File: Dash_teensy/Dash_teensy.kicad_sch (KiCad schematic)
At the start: 72 parts, among them J1 J1B1211CCD, J10 2060-452_998-404, J11 2060-452_998-404, J12 J1B1211CCD, J13 BM04B-GHS-TBT_LF__SN_, J14 BM04B-GHS-TBT_LF__SN_, J15 2060-452_998-404, J2 2060-452_998-404, J3 2060-452_998-404, J4 2060-452_998-404, J5 2060-452_998-404, J6 2060-452_998-404, J7 2060-452_998-404, J8 J1B1211CCD, J9 2060-452_998-404, U1 DEV-16771, U10 MCP2562FDT-E/SN, U11 MCP2562FDT-E/SN, U12 MCP2562FDT-E/SN, U2 DEV-16771, U3 DEV-16771, U4 MCP2562FDT-E/SN, U5 MCP2562FDT-E/SN, U6 MCP2562FDT-E/SN, U7 MCP2562FDT-E/SN, U8 MCP2562FDT-E/SN, U9 MCP2562FDT-E/SN

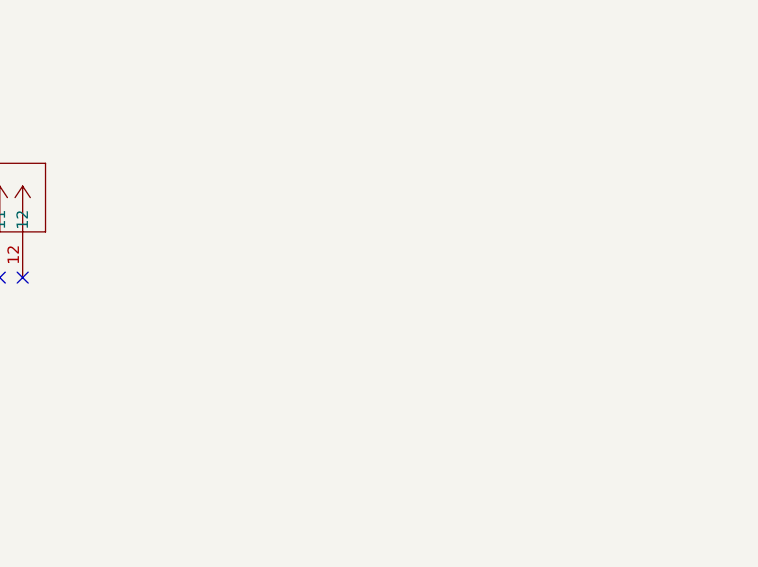
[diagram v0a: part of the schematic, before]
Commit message: figured out placement
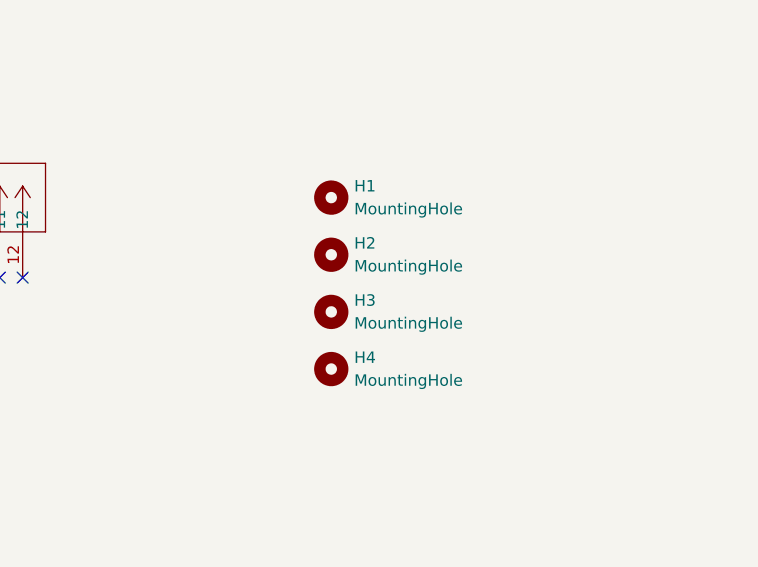
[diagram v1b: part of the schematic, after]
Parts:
- added H1, H2, H3, H4: MountingHole, MountingHole:MountingHole_3.2mm_M3_DIN965_Pad, symbol Mechanical:MountingHole
